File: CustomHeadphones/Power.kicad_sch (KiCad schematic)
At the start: 1 part

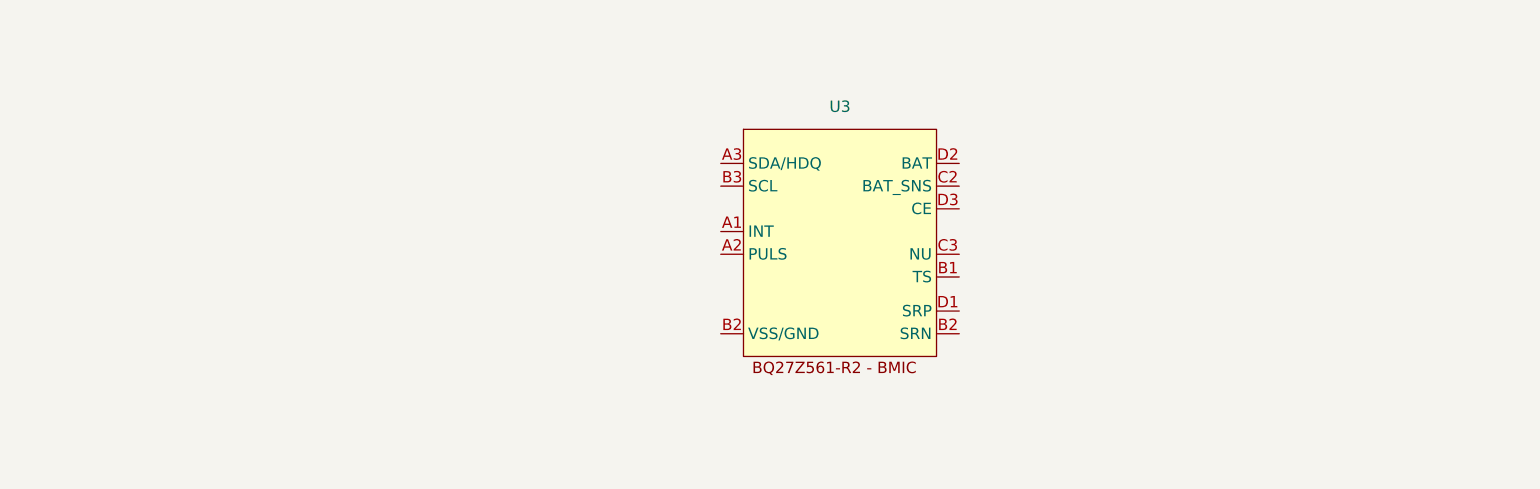
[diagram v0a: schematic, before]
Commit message: LDO circuitry and USB connector symbol
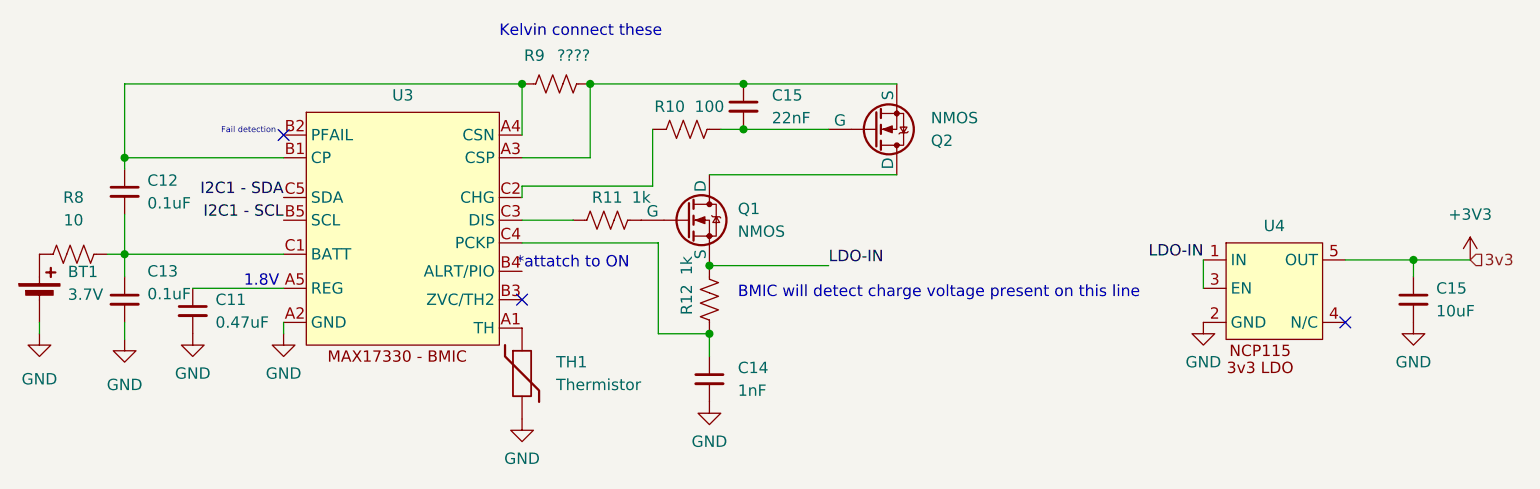
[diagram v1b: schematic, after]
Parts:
- removed U3: ~, symbol CustomSymbols:BQ27Z561-R2
- added BT1: 3.7V, symbol Device:Battery_Cell
- added C11: 0.47uF, symbol Device:C_Small
- added C12, C13: 0.1uF, symbol Device:C_Small
- added C14: 1nF, symbol Device:C_Small
- added C15: 22nF, symbol Device:C_Small
- added C15: 10uF, symbol Device:C_Small
- added Q1, Q2: NMOS, symbol Simulation_SPICE:NMOS
- added R10: 100, symbol Device:R_US
- added R11, R12: 1k, symbol Device:R_US
- added R8: 10, symbol Device:R_US
- added R9: ????, symbol Device:R_US
- added TH1: Thermistor, symbol Device:Thermistor
- added U3: ~, symbol CustomSymbols:MAX17330
- added U4: ~, symbol CustomSymbols:NCP115ASN330T2G
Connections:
- new net: C14.1, R12.1, U3.C4 (PCKP)
- new net: R10.1, U3.C2 (CHG)
- new net: C15.2, Q2.2 (G), R10.2
- new net: C15.1, Q2.3 (S), R9.1, U3.A3 (CSP)
- new net: TH1.1, U3.A1 (TH)
- new net: C12.1, R9.2, U3.A4 (CSN), U3.B1 (CP)
- new net: C11.1, U3.A5 (REG)
- new net: C12.2, C13.1, R8.2, U3.C1 (BATT)
- new net: R11.1, U3.C3 (DIS)
- new net: BT1.1 (+), R8.1
- new net: Q1.2 (G), R11.2
- new net: Q1.1 (D), Q2.1 (D)
- new net +3V3: C15.1, U4.5 (OUT)
- new net GND: BT1.2 (-), C11.2, C13.2, C14.2, C15.2, TH1.2, U3.A2 (GND), U4.2 (GND)
- new net I2C1 - SCL: U3.B5 (SCL)
- new net I2C1 - SDA: U3.C5 (SDA)
- new net LDO-IN: Q1.3 (S), R12.2, U4.1 (IN), U4.3 (EN)
- no-connect marks 0 -> 3
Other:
- note added: "*attatch to ON"
- note added: "1.8V"
- note added: "BMIC will detect charge voltage present on this line"
- note added: "Fail detection"
- note added: "Kelvin connect these"

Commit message: sync, more work on charging
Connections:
- net LDO-IN renamed VPACK
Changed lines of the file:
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@@
     (effects (font (size 1.27 1.27)) (justify right bottom))
+  )
+  (hierarchical_label "VPACK" (shape input) (at 128.27 55.88 90) (fields_autoplaced)
+    (effects (font (size 1.27 1.27)) (justify left))
   )
   (hierarchical_label "3v3" (shape input) (at 201.295 55.245 0) (fields_autoplaced)
